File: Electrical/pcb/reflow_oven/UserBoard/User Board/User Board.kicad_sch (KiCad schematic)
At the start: 27 parts, among them J1 USER BOARD DISPLAY, J2 USER BOARD BUTTON, Q1 DMN13H750S, SW1 UP, SW2 LT, SW3 DWN, SW4 RT, SW5 OK

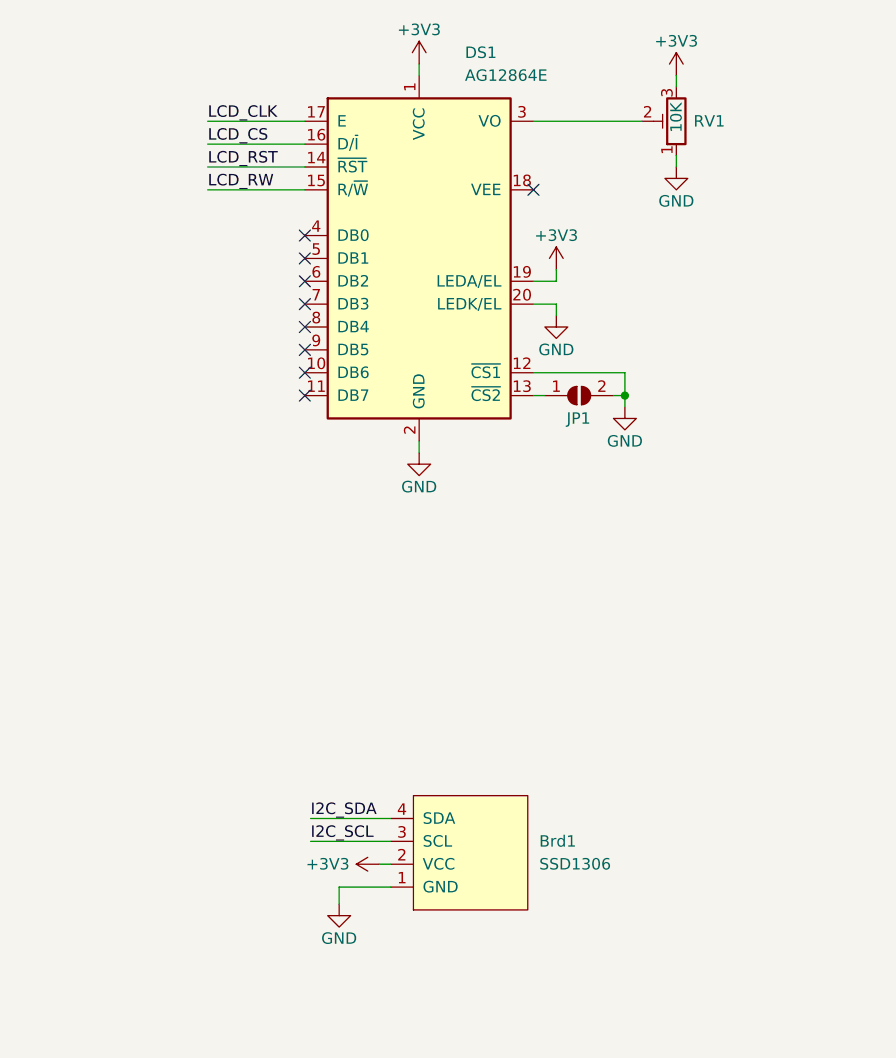
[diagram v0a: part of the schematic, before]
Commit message: fix
changed display footprint
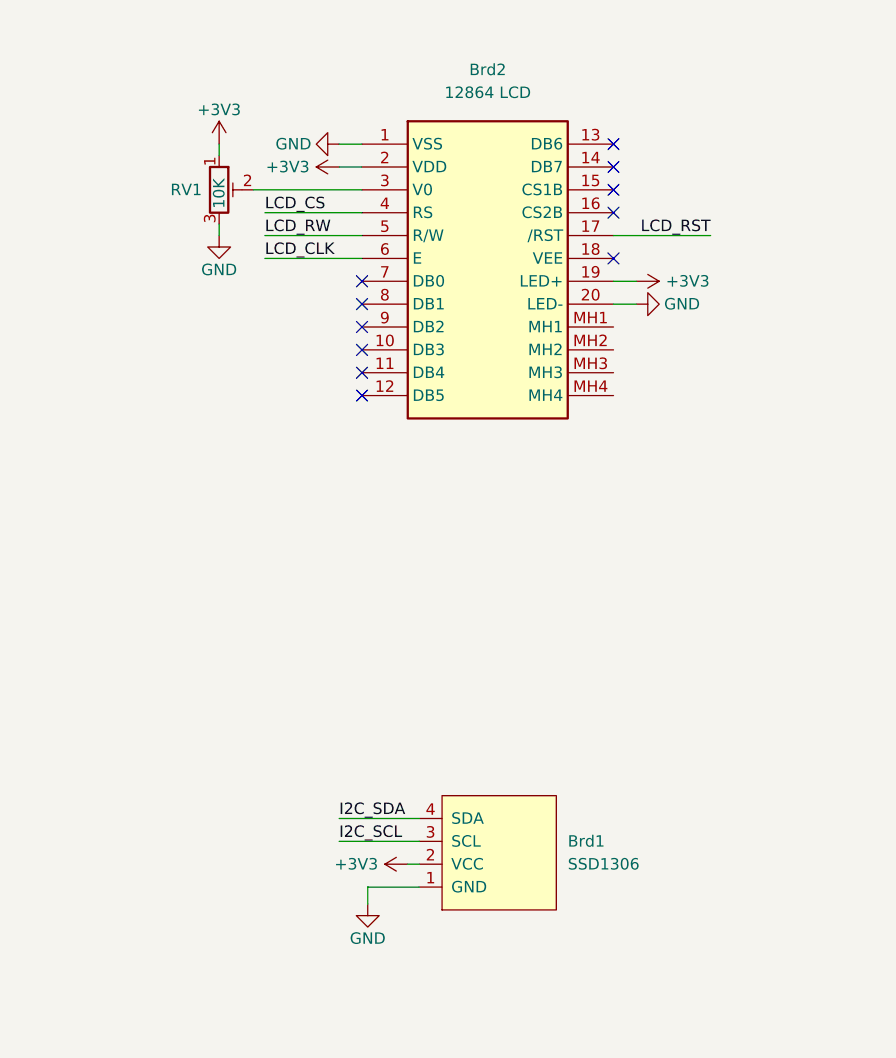
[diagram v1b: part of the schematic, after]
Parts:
- removed DS1: AG12864E, Display:AG12864E, symbol Display_Graphic:AG12864E
- removed JP1: SolderJumper_2_Open, Jumper:SolderJumper-2_P1.3mm_Open_RoundedPad1.0x1.5mm, symbol Jumper:SolderJumper_2_Open
- added Brd2: 12864 LCD, footprint_lib:NHD12864AZFSWGBWVZ, symbol comp_lib:NHD-12864AZ-FSW-GBW-VZ
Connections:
- net +3V3: now also RV1.1, Brd2.19 (LED+), Brd2.2 (VDD); no longer RV1.3
- net GND: now also RV1.3, Brd2.1 (VSS), Brd2.20 (LED-); no longer RV1.1
- net LCD_CLK: now also Brd2.6 (E)
- net LCD_CS: now also Brd2.4 (RS)
- net LCD_RST: now also Brd2.17 (/RST)
- net LCD_RW: now also Brd2.5 (R/W)
- net at RV1.2: now also Brd2.3 (V0)
- no-connect marks 9 -> 11
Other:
- moved on the sheet: Brd1
